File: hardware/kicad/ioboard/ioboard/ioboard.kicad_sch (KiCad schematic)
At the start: 0 parts

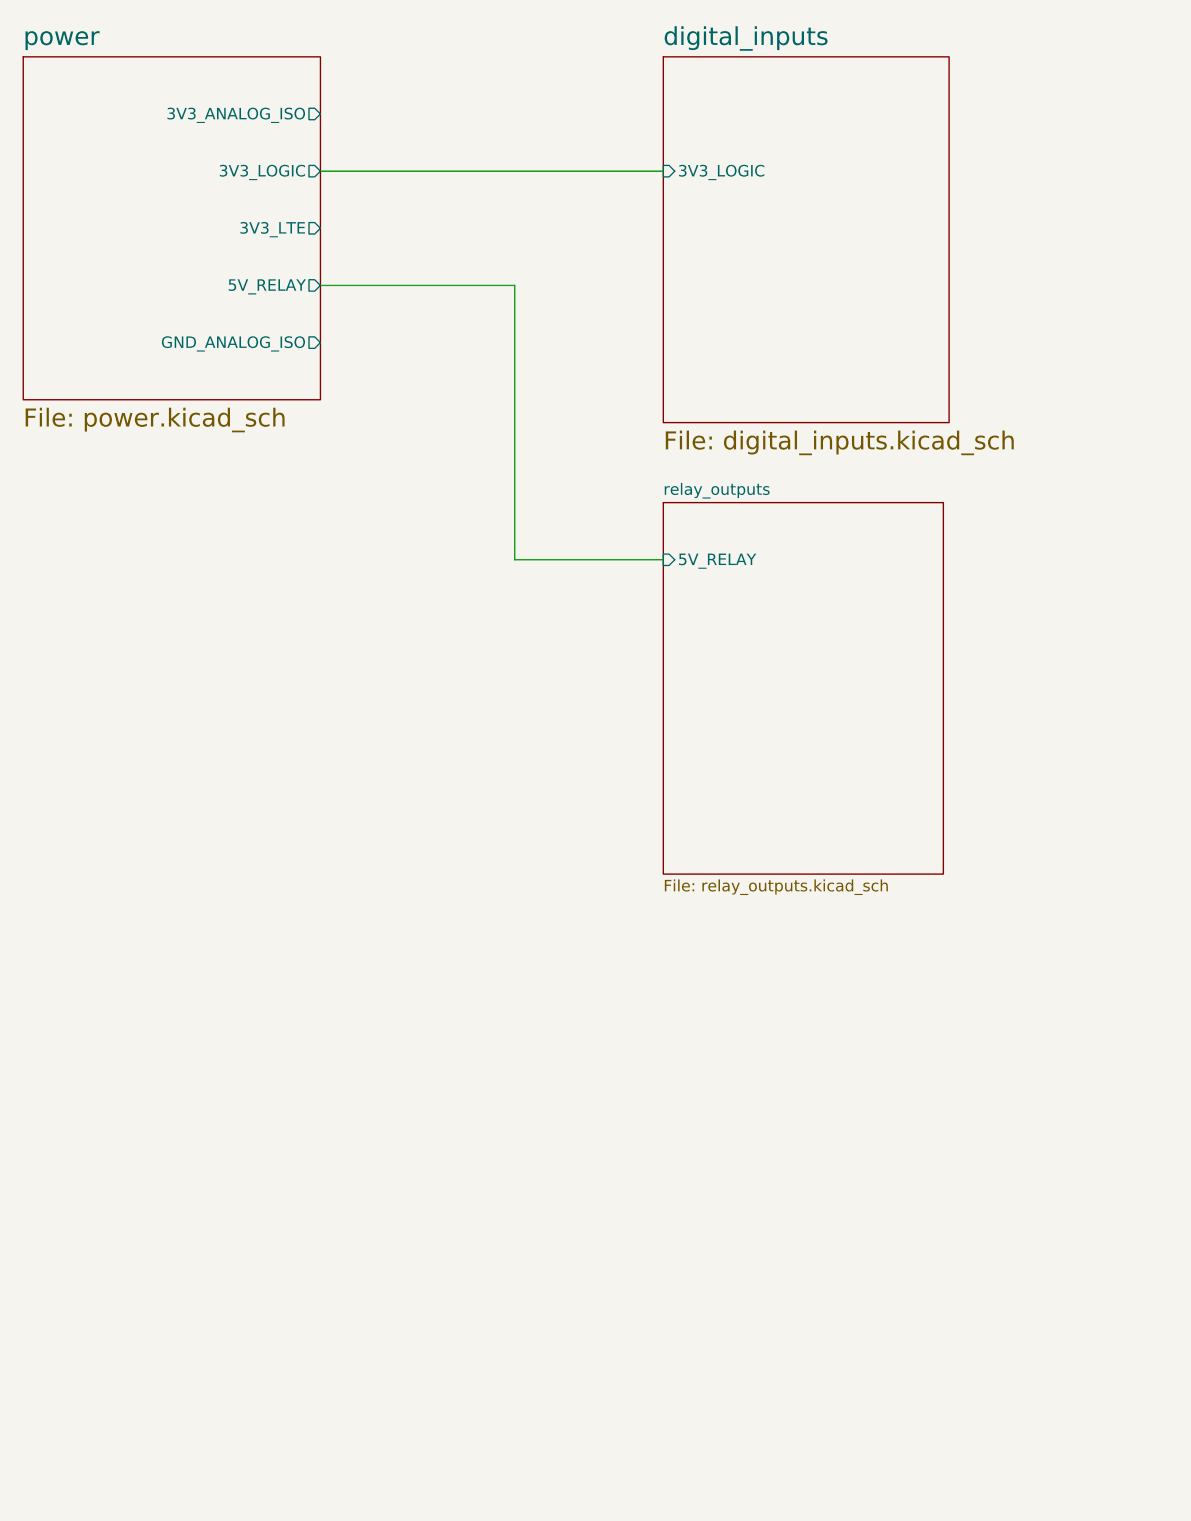
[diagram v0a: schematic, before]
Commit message: power: add isolated 15V rail (U7, RK-0515S) for analog output gain stage
Solves the 15V problem flagged during analog-io's design: U13's output gain
amplifier needed an isolated 15V supply, and 15V_ANALOG_ISO had already been
placed as a hierarchical label on its V+ pin with nothing driving it.

- Added U7 (Recom RK-0515S, isolated DC-DC, 4.5-5.5V in / 15V out / 66mA,
  3kVDC isolation) to power.kicad_sch. Verified wiring: +VIN->5V_RELAY,
  -VIN->GND_LOGIC, +VOUT->new hierarchical label 15V_ANALOG_ISO,
  -VOUT->GND_ANALOG_ISO. Confirmed -VIN and -VOUT resolve to two distinct
  nets (isolation preserved), via a from-scratch KiCad connectivity script
  (S-expression parser + coordinate-transform pin geometry + union-find net
  reconstruction) extended this session to handle single-unit symbols using
  KiCad's "_0_0" sub-symbol convention (RK-0515S), and to detect labels that
  touch a wire mid-segment rather than at an endpoint (both 5V_RELAY and
  GND_LOGIC connect to U7 this way).
- Imported the RK-0515S KiCad symbol/footprint/3D-model library
  (hardware/kicad/ioboard/libs/RK-0515S/) and registered it in
  ioboard/sym-lib-table.
- Completed the root-sheet routing in ioboard.kicad_sch: added a
  15V_ANALOG_ISO output pin to the power sheet symbol and wired it through
  to analog_io's pre-existing 15V_ANALOG_ISO input pin. This diff also
  carries the analog_io sheet symbol's own placement (pins, position) since
  the wire terminates on it and KiCad records both in the same file -
  analog_io.kicad_sch's actual circuit content is intentionally left
  untracked/excluded, as it belongs to that subsystem's own not-yet-merged
  branch.
- docs/subsystems/power.md: added the 15V-ANALOG-ISO rail and RK-0515S
  module selection entry; corrected the LM2904 load-budget row (was a single
  row on 3.3V-LOGIC with an imprecise per-amp figure - split into U12 on
  3.3V-ANALOG-ISO and U13 on 15V-ANALOG-ISO, both at the TI-datasheet-
  verified 0.7-1.2 mA dual-package draw); updated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
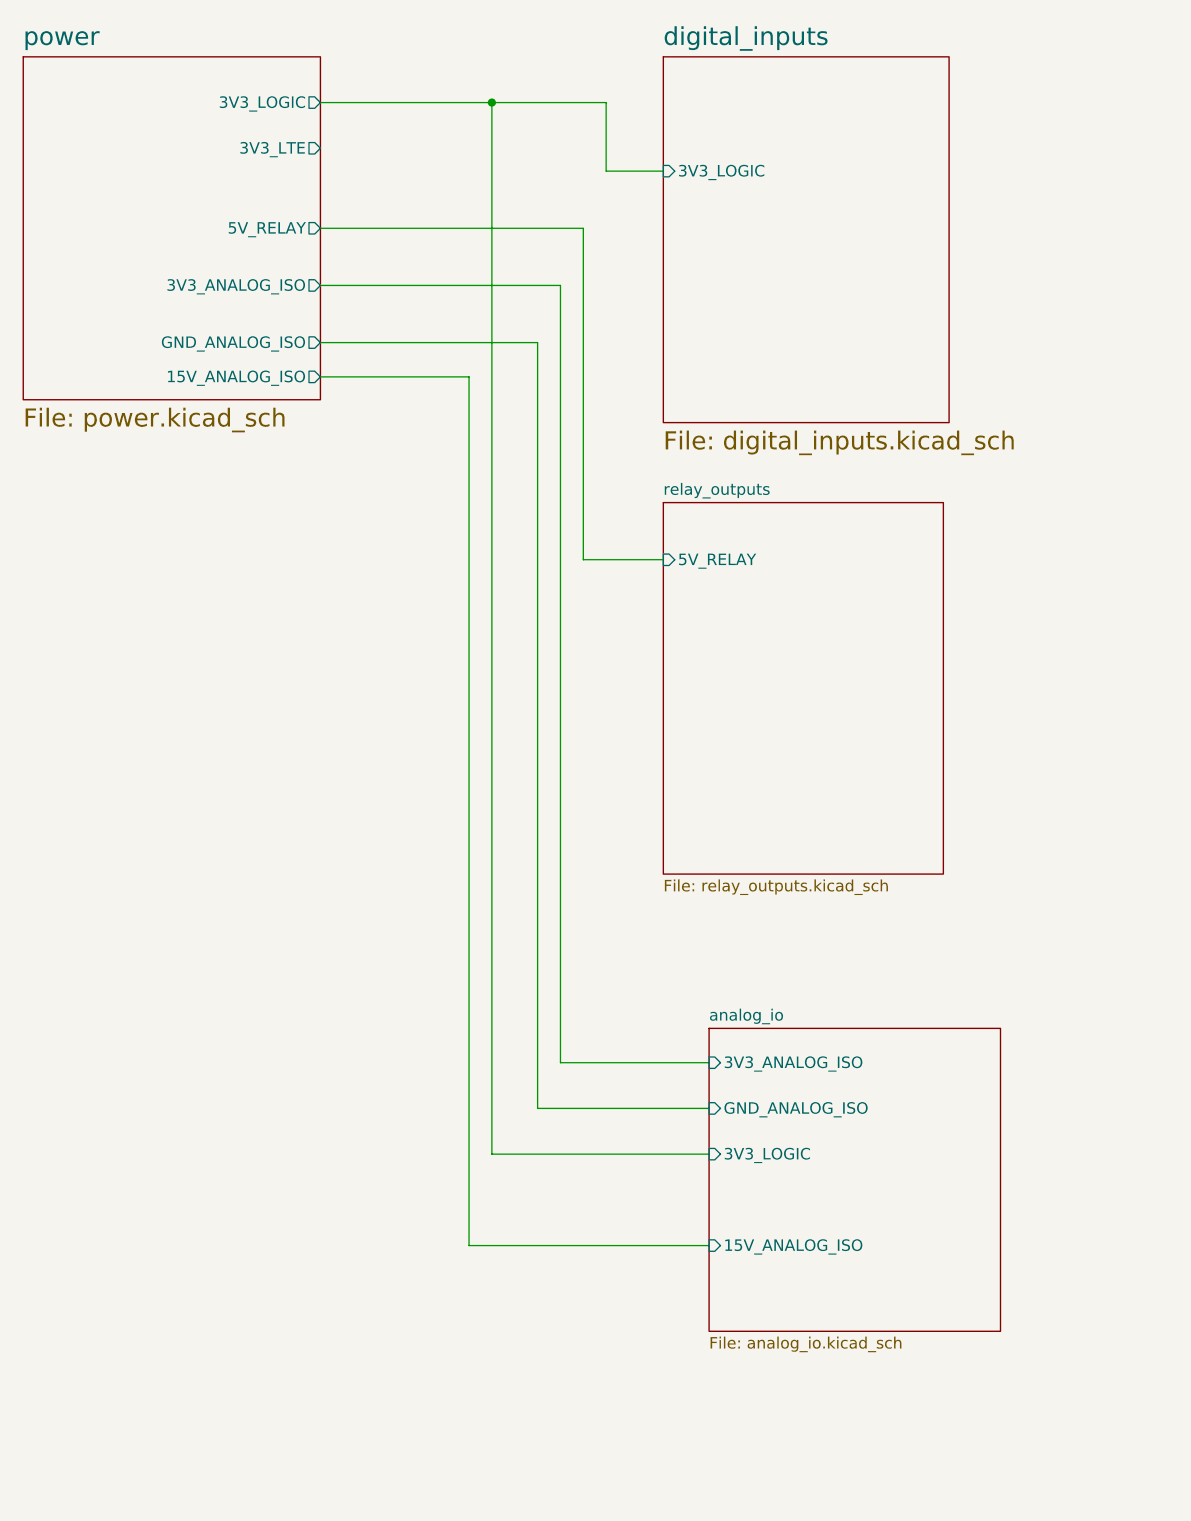
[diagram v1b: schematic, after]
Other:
- added sheet analog_io (analog_io.kicad_sch)
- sheet power ports: added 15V_ANALOG_ISO; removed none
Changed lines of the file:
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@@
 	(generator_version "9.0")
 	(paper "A4")
-	(wire
-		(pts
-			(xy 102.87 88.9) (xy 86.36 88.9)
-		)
-		(stroke
-			(width 0)
-			(type default)
-		)
-	)
-	(wire
-		(pts
-			(xy 64.77 45.72) (xy 102.87 45.72)
-		)
-		(stroke
-			(width 0)
-			(type default)
-		)
-	)
-	(wire
-		(pts
-			(xy 86.36 58.42) (xy 86.36 88.9)
-		)
-		(stroke
-			(width 0)
-			(type default)
-		)
-	)
-	(wire
-		(pts
-			(xy 64.77 58.42) (xy 86.36 58.42)
+	(junction
+		(at 83.82 38.1)
+		(diameter 0)
+		(color 0 0 0 0)
+	)
+	(wire
+		(pts
+			(xy 81.28 68.58) (xy 81.28 165.1)
+		)
+		(stroke
+			(width 0)
+			(type default)
+		)
+	)
+	(wire
+		(pts
+			(xy 88.9 64.77) (xy 88.9 149.86)
+		)
+		(stroke
+			(width 0)
+			(type default)
+		)
+	)
+	(wire
+		(pts
+			(xy 102.87 88.9) (xy 93.98 88.9)
+		)
+		(stroke
+			(width 0)
+			(type default)
+		)
+	)
+	(wire
+		(pts
+			(xy 64.77 58.42) (xy 91.44 58.42)
+		)
+		(stroke
+			(width 0)
+			(type default)
+		)
+	)
+	(wire
+		(pts
+			(xy 64.77 52.07) (xy 93.98 52.07)
+		)
+		(stroke
+			(width 0)
+			(type default)
+		)
+	)
+	(wire
+		(pts
+			(xy 96.52 45.72) (xy 102.87 45.72)
+		)
+		(stroke
+			(width 0)
+			(type default)
+		)
+	)
+	(wire
+		(pts
+			(xy 93.98 52.07) (xy 93.98 88.9)
+		)
+		(stroke
+			(width 0)
+			(type default)
+		)
+	)
+	(wire
+		(pts
+			(xy 88.9 149.86) (xy 107.95 149.86)
+		)
+		(stroke
+			(width 0)
+			(type default)
+		)
+	)
+	(wire
+		(pts
+			(xy 81.28 165.1) (xy 107.95 165.1)
+		)
+		(stroke
+			(width 0)
+			(type default)
+		)
+	)
+	(wire
+		(pts
+			(xy 64.77 38.1) (xy 83.82 38.1)
+		)
+		(stroke
+			(width 0)
+			(type default)
+		)
+	)
+	(wire
+		(pts
+			(xy 83.82 154.94) (xy 83.82 38.1)
+		)
+		(stroke
+			(width 0)
+			(type default)
+		)
+	)
+	(wire
+		(pts
+			(xy 64.77 64.77) (xy 88.9 64.77)
+		)
+		(stroke
+			(width 0)
+			(type default)
+		)
+	)
+	(wire
+		(pts
+			(xy 91.44 58.42) (xy 91.44 144.78)
+		)
+		(stroke
+			(width 0)
+			(type default)
+		)
+	)
+	(wire
+		(pts
+			(xy 91.44 144.78) (xy 107.95 144.78)
+		)
+		(stroke
+			(width 0)
+			(type default)
+		)
+	)
+	(wire
+		(pts
+			(xy 107.95 154.94) (xy 83.82 154.94)
+		)
+		(stroke
+			(width 0)
+			(type default)
+		)
+	)
+	(wire
+		(pts
+			(xy 96.52 38.1) (xy 96.52 45.72)
+		)
+		(stroke
+			(width 0)
+			(type default)
+		)
+	)
+	(wire
+		(pts
+			(xy 83.82 38.1) (xy 96.52 38.1)
+		)
+		(stroke
+			(width 0)
+			(type default)
+		)
+	)
+	(wire
+		(pts
+			(xy 64.77 68.58) (xy 81.28 68.58)
 		)
 		(stroke
@@
 		)
 		(pin "3V3_ANALOG_ISO" output
-			(at 64.77 39.37 0)
+			(at 64.77 58.42 0)
 			(effects
 				(font
@@
 		)
 		(pin "3V3_LOGIC" output
-			(at 64.77 45.72 0)
+			(at 64.77 38.1 0)
 			(effects
 				(font
@@
 		)
 		(pin "3V3_LTE" output
+			(at 64.77 43.18 0)
+			(effects
+				(font
+					(size 1.27 1.27)
+				)
+				(justify right)
+			)
+		)
+		(pin "5V_RELAY" output
 			(at 64.77 52.07 0)
-			(effects
-				(font
-					(size 1.27 1.27)
-				)
-				(justify right)
-			)
-		)
-		(pin "5V_RELAY" output
-			(at 64.77 58.42 0)
 			(effects
 				(font
@@
 		(pin "GND_ANALOG_ISO" output
 			(at 64.77 64.77 0)
+			(effects
+				(font
+					(size 1.27 1.27)
+				)
+				(justify right)
+			)
+		)
+		(pin "15V_ANALOG_ISO" output
+			(at 64.77 68.58 0)
 			(effects
 				(font
@@
 				)
 			)
+		)
+	)
+	(sheet
+		(at 107.95 140.97)
+		(size 32.385 33.655)
+		(exclude_from_sim no)
+		(in_bom yes)
+		(on_board yes)
+		(dnp no)
+		(fields_autoplaced yes)
+		(stroke
+			(width 0.1524)
+			(type solid)
+		)
+		(fill
+			(color 0 0 0 0.0000)
+		)
+		(property "Sheetname" "analog_io"
+			(at 107.95 140.2584 0)
+			(effects
+				(font
+					(size 1.27 1.27)
+				)
+				(justify left bottom)
+			)
+		)
+		(property "Sheetfile" "analog_io.kicad_sch"
+			(at 107.95 175.2096 0)
+			(effects
+				(font
+					(size 1.27 1.27)
+				)
+				(justify left top)
+			)
+		)
+		(pin "3V3_ANALOG_ISO" input
+			(at 107.95 144.78 180)
+			(effects
+				(font
+					(size 1.27 1.27)
+				)
+				(justify left)
+			)
+		)
+		(pin "15V_ANALOG_ISO" input
+			(at 107.95 165.1 180)
+			(effects
+				(font
+					(size 1.27 1.27)
+				)
+				(justify left)
+			)
+		)
+		(pin "GND_ANALOG_ISO" input
+			(at 107.95 149.86 180)
+			(effects
+				(font
+					(size 1.27 1.27)
+				)
+				(justify left)
+			)
+		)
+		(pin "3V3_LOGIC" input
+			(at 107.95 154.94 180)
+			(effects
+				(font
+					(size 1.27 1.27)
+				)
+				(justify left)
+			)
+		)
+		(instances
+			(project "ioboard"
+				(path "/a0fa9f92-ef51-408b-9617-1545f9e9dad8"
+					(page "5")
+				)
+			)

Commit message: Recover rs485.kicad_sch and its root-sheet integration
Both the rs485 sheet block in ioboard.kicad_sch and the rs485.kicad_sch
file itself had disappeared from the working tree sometime between
today's 09:00 and 10:52 KiCad auto-backups (isolated removal - diffing
the two backups showed nothing else changed). Recovered by extracting
both files from ioboard-backups/ioboard-2026-09-10_090053.zip, verified
byte-for-byte against that backup and structurally intact (balanced
s-expression, no corruption). Sheet pins (3V3_LOGIC, RS485_RXD,
RS485_TXD) match rs485.md's documented Step 4 capture exactly.

Co-Authored-By: Claude Sonnet 5 <noreply@anthropic.com>
Claude-Session: https://claude.ai/code/session_011Mk4ACKLUzGL8p2SUjrweQ
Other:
- added sheet rs232 (rs232.kicad_sch)
- added sheet rs485 (rs485.kicad_sch)
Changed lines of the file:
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@@
 	(paper "A4")
+	(junction
+		(at 78.74 38.1)
+		(diameter 0)
+		(color 0 0 0 0)
+	)
 	(junction
 		(at 83.82 38.1)
@@
 		(color 0 0 0 0)
 	)
+	(junction
+		(at 62.484 113.03)
+		(diameter 0)
+		(color 0 0 0 0)
+	)
 	(wire
 		(pts
@@
 	(wire
 		(pts
-			(xy 64.77 38.1) (xy 83.82 38.1)
+			(xy 78.74 38.1) (xy 83.82 38.1)
+		)
+		(stroke
+			(width 0)
+			(type default)
+		)
+	)
+	(wire
+		(pts
+			(xy 78.74 113.03) (xy 78.74 38.1)
+		)
+		(stroke
+			(width 0)
+			(type default)
+		)
+	)
+	(wire
+		(pts
+			(xy 62.484 113.03) (xy 78.74 113.03)
+		)
+		(stroke
+			(width 0)
+			(type default)
+		)
+	)
+	(wire
+		(pts
+			(xy 64.77 38.1) (xy 78.74 38.1)
 		)
 		(stroke
@@
 		(pts
 			(xy 91.44 144.78) (xy 107.95 144.78)
+		)
+		(stroke
+			(width 0)
+			(type default)
+		)
+	)
+	(wire
+		(pts
+			(xy 62.23 113.03) (xy 62.484 113.03)
 		)
 		(stroke
@@
 				)
 			)
+		)
+	)
+	(sheet
+		(at 31.242 104.648)
+		(size 31.242 44.958)
+		(exclude_from_sim no)
+		(in_bom yes)
+		(on_board yes)
+		(dnp no)
+		(fields_autoplaced yes)
+		(stroke
+			(width 0.1524)
+			(type solid)
+		)
+		(fill
+			(color 0 0 0 0.0000)
+		)
+		(property "Sheetname" "rs485"
+			(at 31.242 103.5714 0)
+			(effects
+				(font
+					(size 2 2)
+				)
+				(justify left bottom)
+			)
+		)
+		(property "Sheetfile" "rs485.kicad_sch"
+			(at 31.242 150.4826 0)
+			(effects
+				(font
+					(size 2 2)
+				)
+				(justify left top)
+			)
+		)
+		(pin "3V3_LOGIC" input
+			(at 62.484 113.03 0)
+			(effects
+				(font
+					(size 1.27 1.27)
+				)
+				(justify right)
+			)
+		)
+		(pin "RS485_RXD" input
+			(at 62.484 118.11 0)
+			(effects
+				(font
+					(size 1.27 1.27)
+				)
+				(justify right)
+			)
+		)
+		(pin "RS485_TXD" input
+			(at 62.484 124.46 0)
+			(effects
+				(font
+					(size 1.27 1.27)
+				)
+				(justify right)
+			)
+		)
+		(instances
+			(project "ioboard"
+				(path "/a0fa9f92-ef51-408b-9617-1545f9e9dad8"
+					(page "6")
+				)
+			)
+		)
+	)
+	(sheet
+		(at 36.068 162.306)
+		(size 29.21 28.702)
+		(exclude_from_sim no)
+		(in_bom yes)
+		(on_board yes)
+		(dnp no)
+		(fields_autoplaced yes)
+		(stroke
+			(width 0.1524)
+			(type solid)
+		)
+		(fill
+			(color 0 0 0 0.0000)
+		)
+		(property "Sheetname" "rs232"
+			(at 36.068 161.5944 0)
+			(effects
+				(font
+					(size 1.27 1.27)
+				)
+				(justify left bottom)
+			)
+		)
+		(property "Sheetfile" "rs232.kicad_sch"
+			(at 36.068 191.5926 0)
+			(effects
+				(font
+					(size 1.27 1.27)
+				)
+				(justify left top)
+			)
+		)
+		(instances
+			(project "ioboard"
+				(path "/a0fa9f92-ef51-408b-9617-1545f9e9dad8"
+					(page "7")
+				)
+			)
